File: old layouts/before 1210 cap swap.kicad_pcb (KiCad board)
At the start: 4 copper layers, 65 x 56 mm, 189 parts, among them J101 Conn_01x01, J102 Conn_01x01, J1101 USB_C_Receptacle, J401 +Vbat, J402 Gnd, J403 A, J404 B, J405 C, J406 Conn_01x03, K101 SERVO, P101 CANBUS, P102 CTRL_SIGNALS, P103 Serial1/tim4, P104 I2C, P106 HALL/Encoder, P801 SWD_DEBUG, P901 I2C, Q401 Q_PNP_BCE, Q501 TPH2R608NH,L1Q, Q502 TPH2R608NH,L1Q, Q503 TPH2R608NH,L1Q, Q504 TPH2R608NH,L1Q, Q601 TPH2R608NH,L1Q, Q602 TPH2R608NH,L1Q, Q603 TPH2R608NH,L1Q, Q604 TPH2R608NH,L1Q, Q701 TPH2R608NH,L1Q, Q702 TPH2R608NH,L1Q, Q703 TPH2R608NH,L1Q, Q704 TPH2R608NH,L1Q, SW801 SW_Push, U201 MAX3051, U301 TPS561201, U401 DRV8353RSRGZT, U801 STM32F40X_LQFP64, X801 8MHz 10ppm, X802 8MHz 10ppm

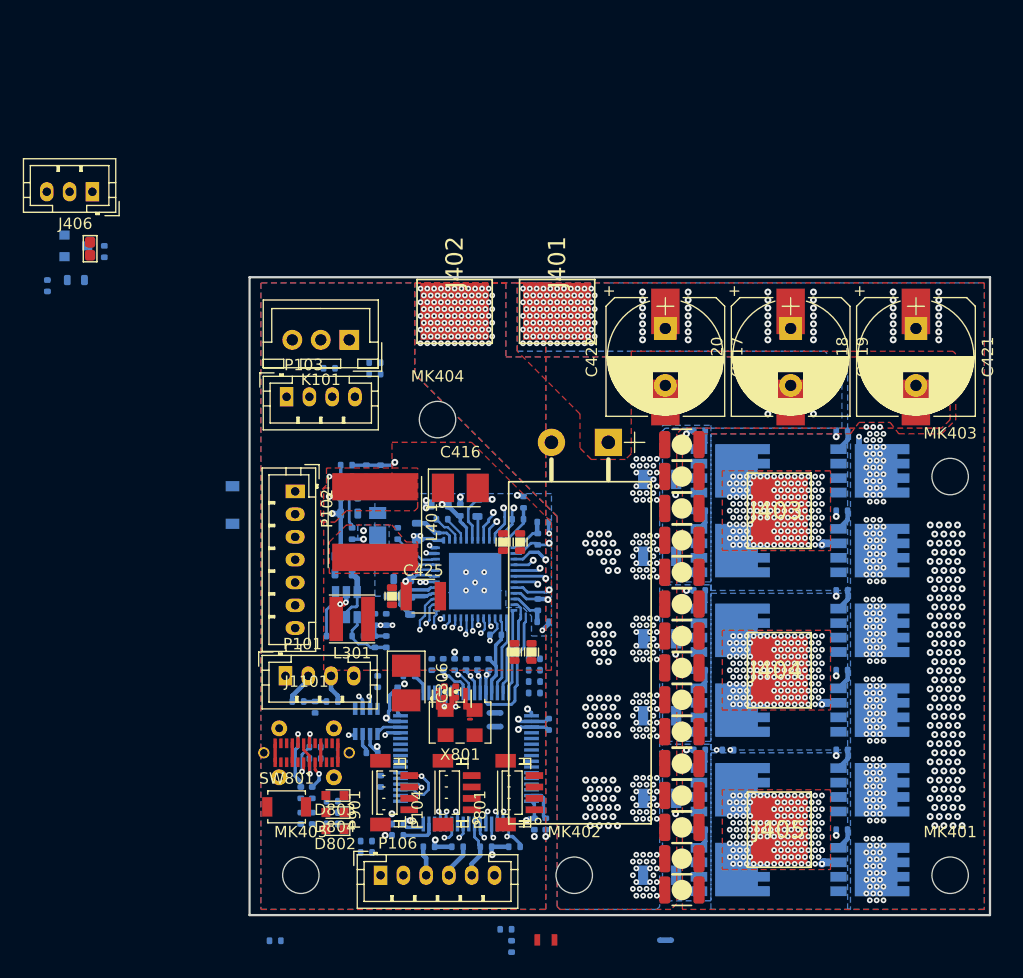
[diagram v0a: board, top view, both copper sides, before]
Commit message: connector layout basically finalised. drv gate layout finished mcu layout starting
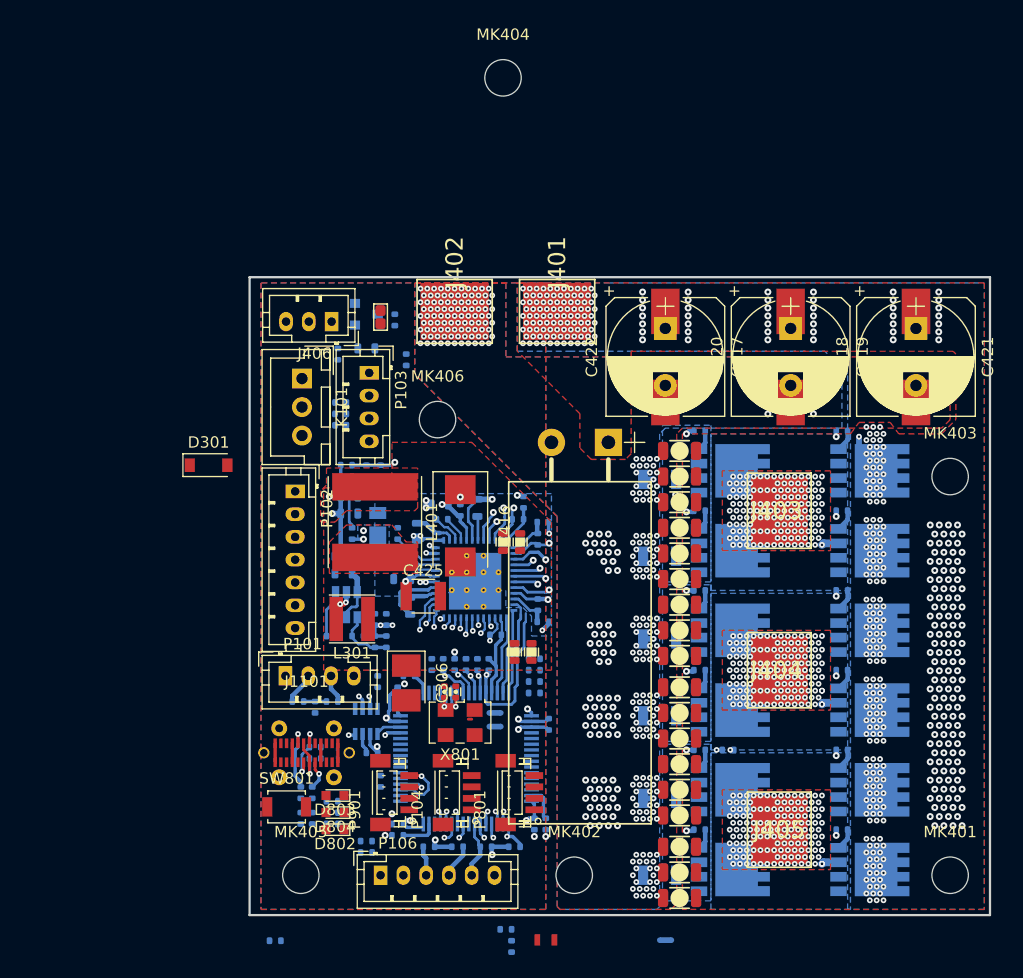
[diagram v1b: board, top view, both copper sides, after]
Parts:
- removed R421: 0Ω, pkl_dipol:R_0603
- removed X802: 8MHz 10ppm, pkl_misc:PRQC
- added C507: 1uF, pkl_dipol:C_1206, F.Cu at (142.2, 150.8)
- added C607: 1uF, pkl_dipol:C_1206, F.Cu at (142.2, 136.8)
- added C707: 1uF, pkl_dipol:C_1206, F.Cu at (142.2, 123.2)
- added MK406: Mounting_Hole, Mounting_Holes:MountingHole_3.2mm_M3_DIN965, F.Cu at (121.0, 116.0)
- C416: value 10uf, 25v -> 47uf, 25v; footprint Capacitors_Tantalum_SMD:CP_Tantalum_Case-B_EIA-3528-21_Reflow -> Capacitors_Tantalum_SMD:CP_Tantalum_Case-V_EIA-7343-20_Reflow
- C502, C503, C504, C505, C506, C602, C603, C604, C605, C606, C702, C703, C704, C705, C706: value 4.7uF -> 1uF; footprint pkl_dipol:C_1210 -> pkl_dipol:C_1206
- D301: moved to F.Cu
- R418: value 1M -> 10k
- moved MK404 30.5 mm to (126.8, 86.0)
- moved JP401 26.2 mm to (116.0, 107.0)
- moved Q401 26.2 mm to (114.8, 106.8)
- moved R418 26.2 mm to (117.2, 107.2)
- moved R419 26.2 mm to (114.8, 109.8)
- moved R420 26.2 mm to (112.2, 110.2)
- moved J406 23.9 mm to (111.7, 107.4)
- moved R403 20.8 mm to (118.2, 110.8), turned to 270 degrees
- moved P103 7.55 mm to (115.0, 111.9), turned to 270 degrees
- moved K101 5.36 mm to (109.1, 112.4), turned to 270 degrees
- moved R101 5.10 mm to (112.5, 116.5)
- moved C101 4.61 mm to (112.5, 115.5)
- moved R102 4.61 mm to (112.5, 114.5)
- moved D301 4.08 mm to (100.9, 120.0), turned to 0 degrees
- moved C416 3.33 mm to (123.0, 125.3), turned to 270 degrees
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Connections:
- net /ADC_BRAKE_R renamed Net-(P102-Pad4)
- net /ADC_THROTTLE_R renamed Net-(P102-Pad3)
- C404 pad 1: /drv_power_stage/BK_VIN -> +BATT
- C425 pad 1: /drv_power_stage/BK_VIN -> +BATT
- R403 pad 1: /drv_power_stage/BK_VIN -> /drv_power_stage/batt_pwr_ctl
- U401 pad 43: /drv_power_stage/BK_VIN -> +BATT
- U801 pad 27: /Microcontroller/BRAKE_SW -> (no net)
- U801 pad 3: (no net) -> /Microcontroller/LED_GREEN
- U801 pad 4: (no net) -> /Microcontroller/LED_RED
- U801 pad 54: /Microcontroller/LED_RED -> (no net)
- U801 pad 57: /Microcontroller/LED_GREEN -> /Microcontroller/BRAKE_SW
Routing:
- net /drv_power_stage/BK_VIN: track 3.12 -> 0.00 mm, vias 1 -> 0
- net +BATT: track 0.00 -> 3.12 mm, vias 463 -> 464
- net +15V: track 20.1 -> 20.8 mm, vias 4 -> 3
- net GNDD: vias 343 -> 338
- net /drv_power_stage/PHASE_C: vias 139 -> 145
- net /drv_power_stage/PHASE_B: vias 139 -> 145
- net /drv_power_stage/PHASE_A: vias 137 -> 143
